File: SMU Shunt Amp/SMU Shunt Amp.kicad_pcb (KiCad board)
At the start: 4 copper layers, 69.9 x 37.6 mm, 32 parts, among them J1 30VDC, J2 Input, J3 Output, U1 OPA189IDBVx, U2 THS3092D

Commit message: Finish layout for design review.
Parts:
- J1: value 30VDC -> 28VDC
- moved J2 0.09 mm to (131.4, 50.8)
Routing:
- net Net-(C8-Pad2): track 0.00 -> 7.23 mm
- net GND: vias 66 -> 127
- net +15V: vias 9 -> 10

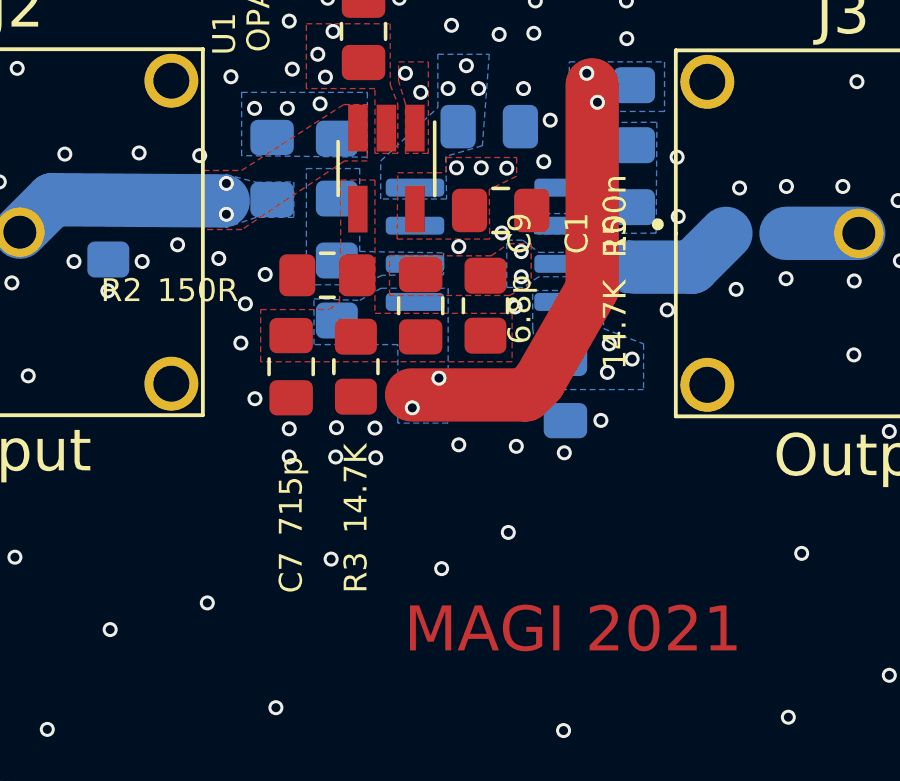
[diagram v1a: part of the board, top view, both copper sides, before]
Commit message: Remove fb caps after more sims. Increase fb resistors in hs loop.
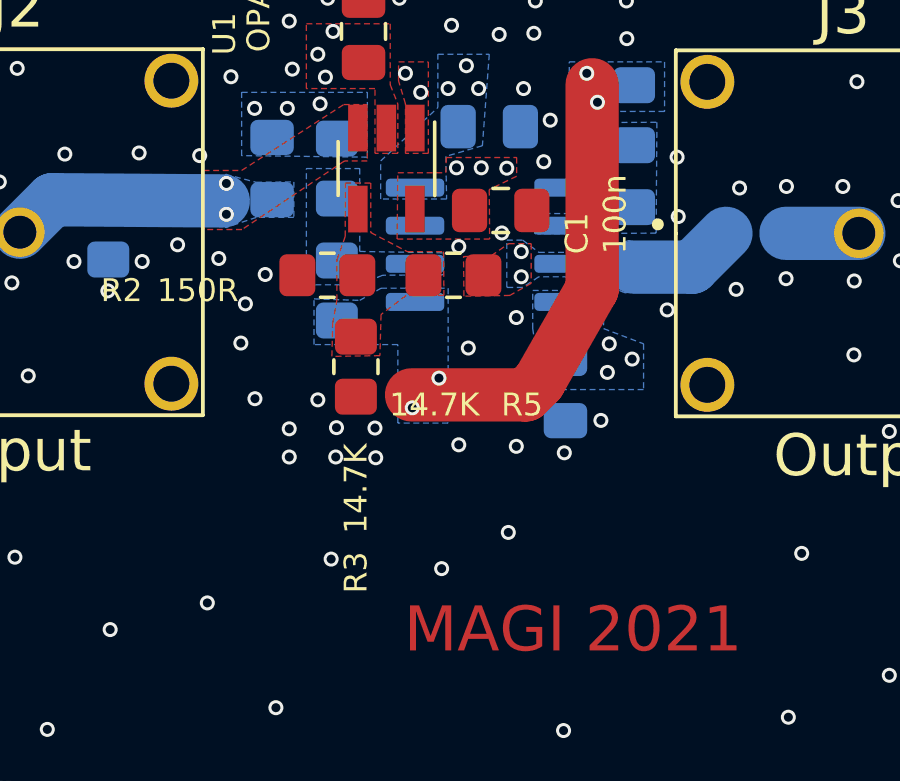
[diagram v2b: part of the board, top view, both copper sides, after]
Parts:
- removed C7: 715p, Capacitor_SMD:C_0805_2012Metric_Pad1.18x1.45mm_HandSolder
- removed C9: 6.8p, Capacitor_SMD:C_0805_2012Metric_Pad1.18x1.45mm_HandSolder
- R7: value 60.4R -> 430R
- R8: value 604R -> 4.3K
- moved R5 1.47 mm to (145.9, 52.2), turned to 180 degrees
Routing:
- net GND: vias 127 -> 129

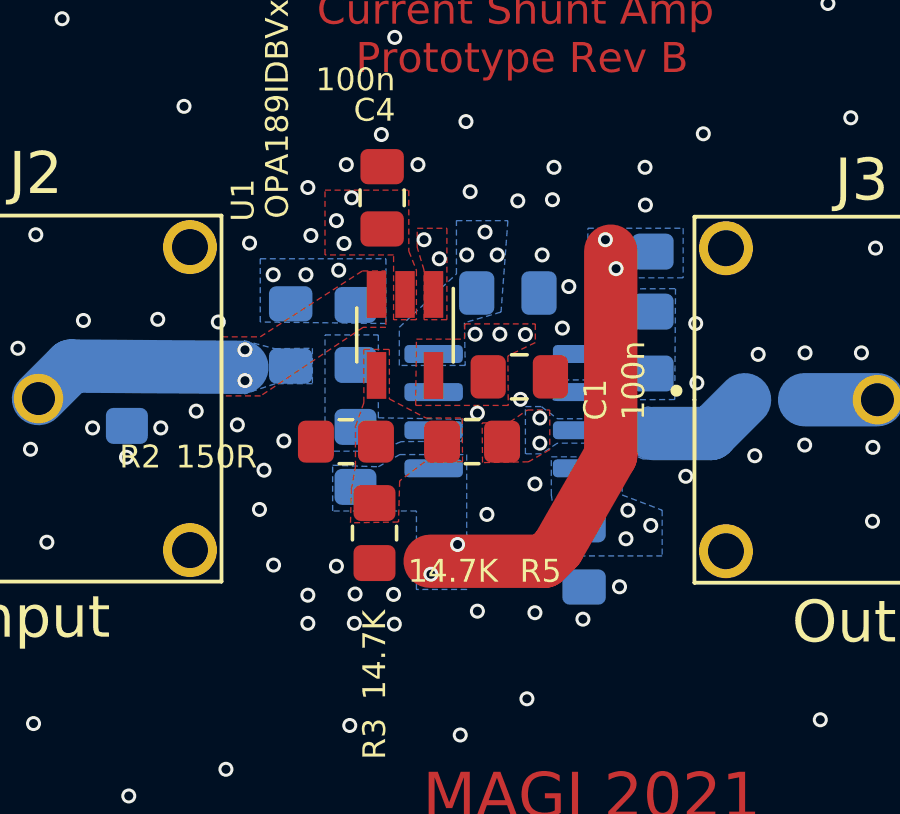
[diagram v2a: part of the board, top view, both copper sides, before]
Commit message: Better grounding for OPA189 +V bypass
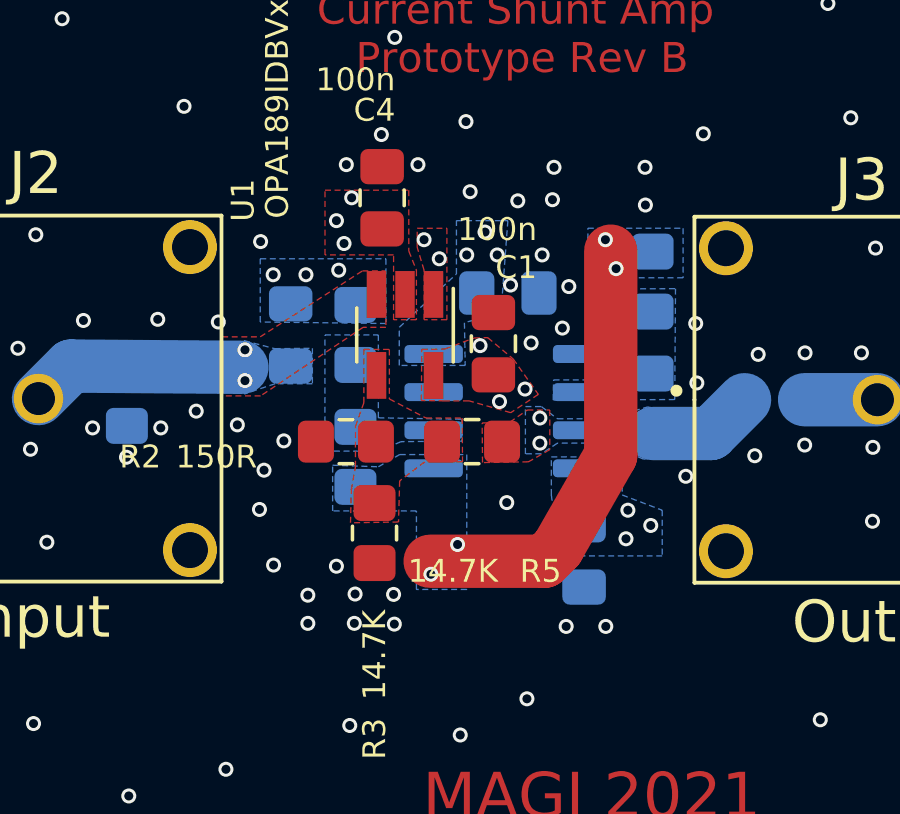
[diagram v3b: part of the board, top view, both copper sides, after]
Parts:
- moved C1 1.40 mm to (146.6, 48.9), turned to 90 degrees
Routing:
- net GND: vias 129 -> 124

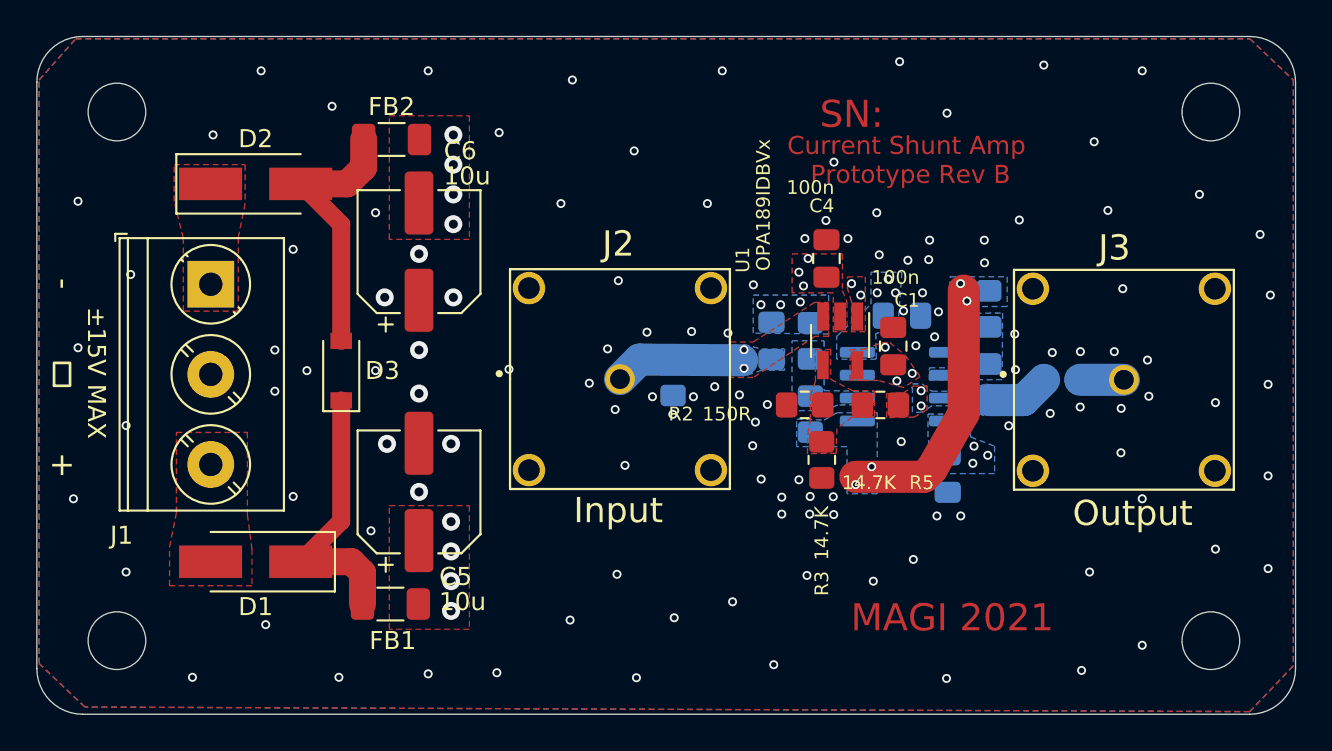
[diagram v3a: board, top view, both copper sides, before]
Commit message: Rev C changes, opa189 now on ths3092 +
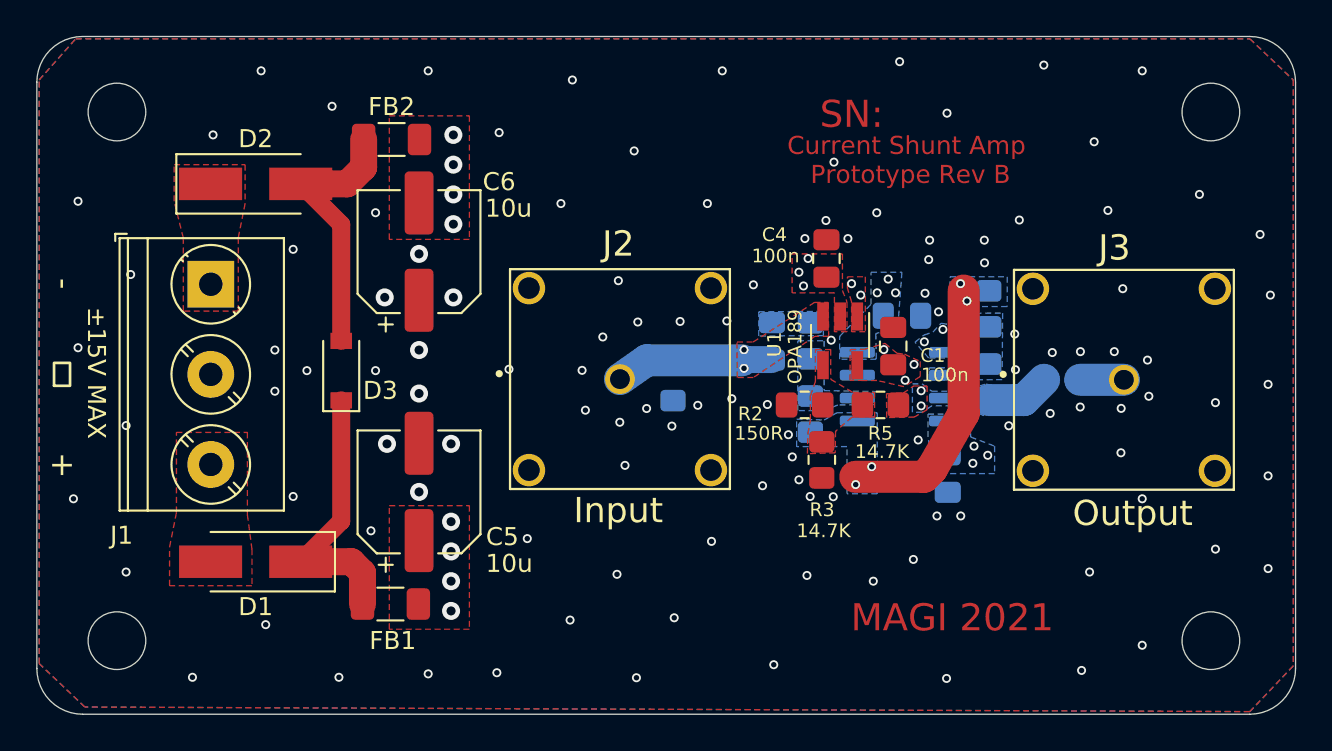
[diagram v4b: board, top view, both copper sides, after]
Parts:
- removed C8: 1u, Capacitor_SMD:C_0805_2012Metric_Pad1.18x1.45mm_HandSolder
- added C7: 1u, Capacitor_SMD:C_0805_2012Metric_Pad1.18x1.45mm_HandSolder, B.Cu at (139.9, 48.7)
- U1: value OPA189IDBVx -> OPA189
- moved R1 0.28 mm to (134.4, 51.0)
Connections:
- R4 pad 2: Net-(C8-Pad1) -> Net-(C7-Pad2)
- U1 pad 1: Net-(C8-Pad1) -> Net-(U1-Pad1)
- U2 pad 5: GND -> Net-(U1-Pad1)
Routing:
- net Net-(U1-Pad1): track 0.00 -> 6.68 mm, vias 0 -> 4
- net Net-(C7-Pad1): track 7.23 -> 8.75 mm
- net Net-(C8-Pad1): vias 5 -> 0
- net GND: vias 124 -> 117
- added copper zone on B.Cu, net Net-(C7-Pad2)
- added copper zone on B.Cu, net Net-(U1-Pad1)
- added copper zone on F.Cu, net Net-(U1-Pad1)
- removed copper zone on B.Cu, net Net-(C7-Pad1)
- removed copper zone on B.Cu, net Net-(C8-Pad1)
- removed copper zone on F.Cu, net Net-(C8-Pad1)
- removed copper zone on In1.Cu, net Net-(C8-Pad1)
